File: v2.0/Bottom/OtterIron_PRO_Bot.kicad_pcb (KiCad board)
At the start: 2 copper layers, 50 x 20.5 mm, 47 parts, among them J1 Conn_01x10, J3 C245, P1 TC2030-CTX, Q1 SS8050, Q2 DMP3017SFG, Q3 SS8050, Q4 BC807, U2 AP2204R-3.3, U4 STM32F072C8Tx, U5 OPA340NA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

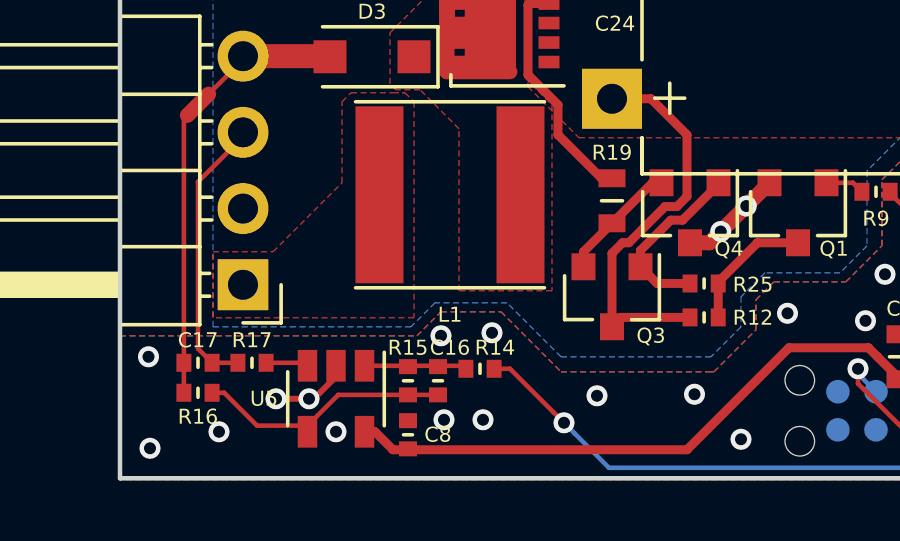
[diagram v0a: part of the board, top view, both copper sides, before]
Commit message: Add missing 3D models
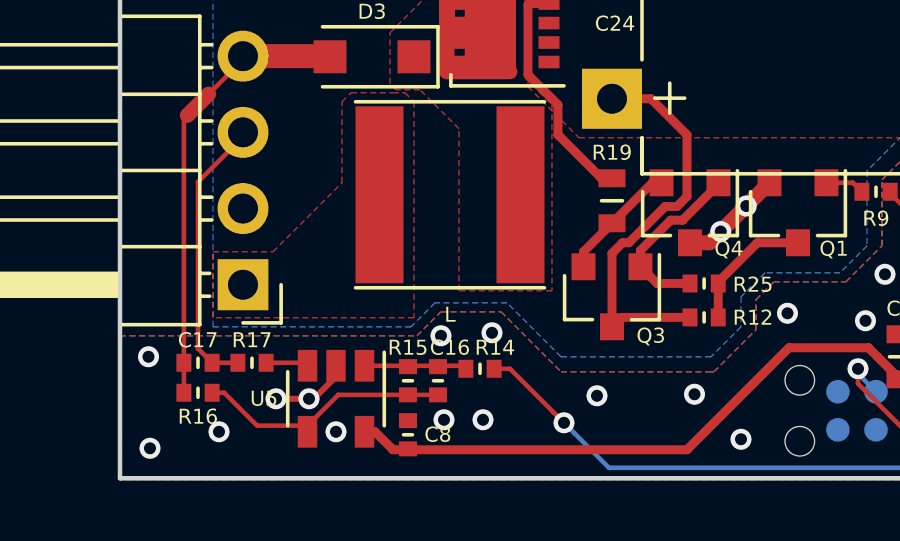
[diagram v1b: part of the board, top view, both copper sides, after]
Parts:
- renumbered L1 to L
